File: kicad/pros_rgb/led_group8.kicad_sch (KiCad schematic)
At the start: 8 parts

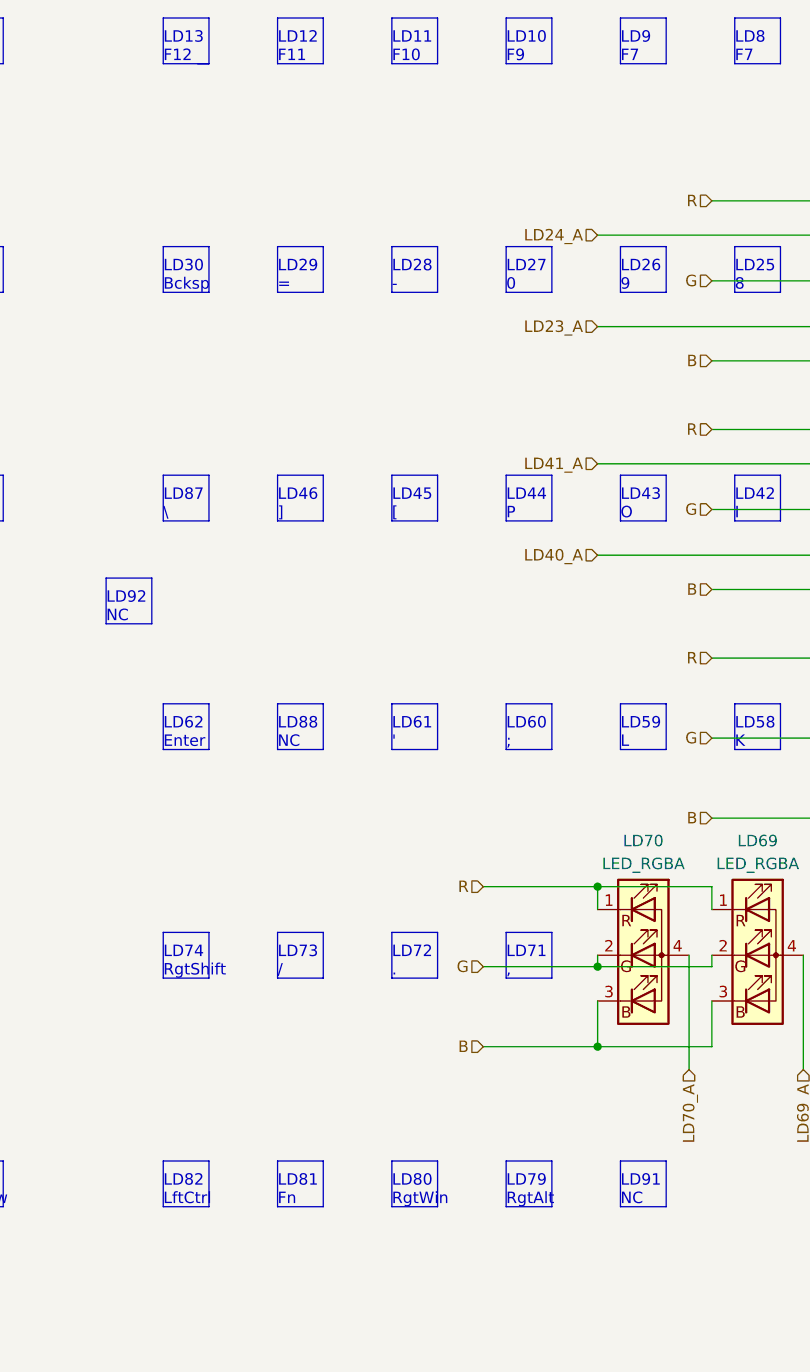
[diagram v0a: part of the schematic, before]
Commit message: kicad/pros_rgb: fix typos
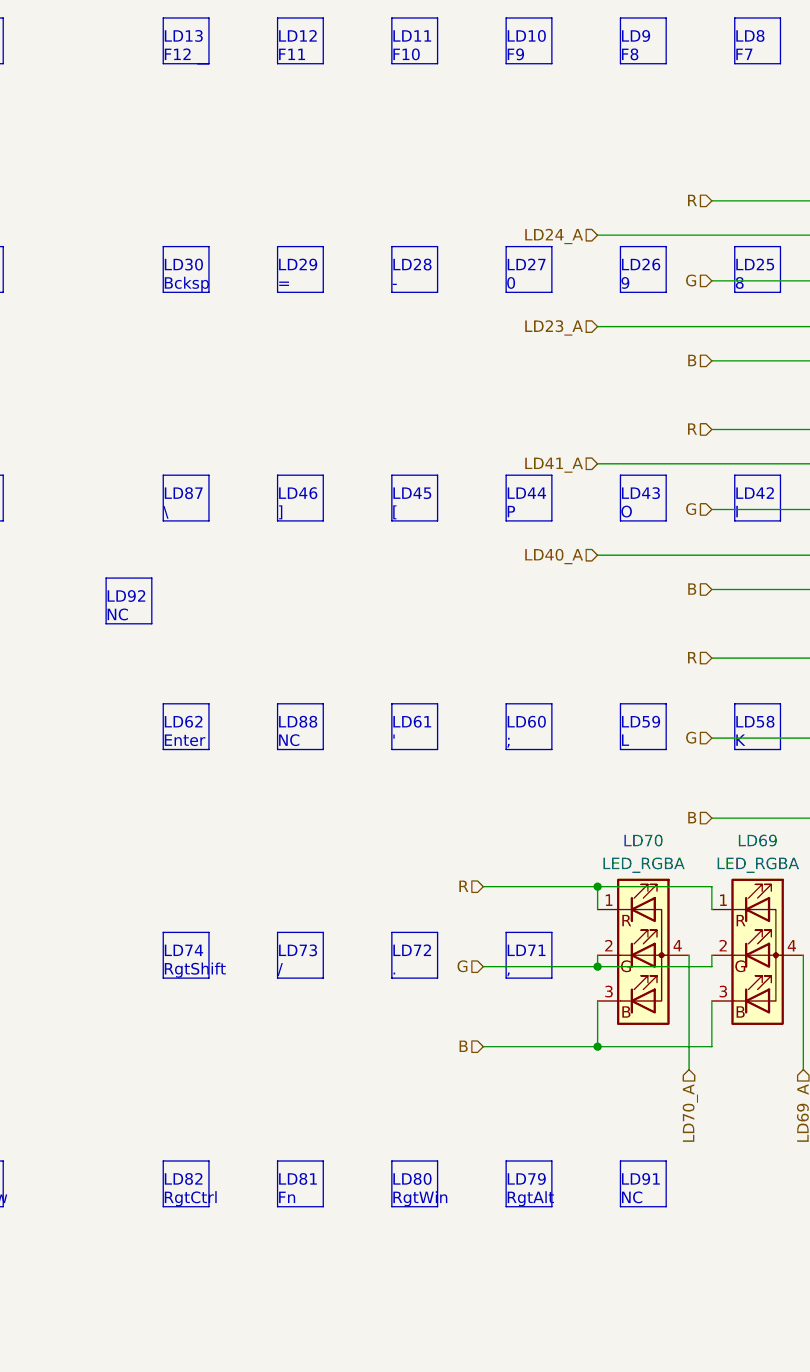
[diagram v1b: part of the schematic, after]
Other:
- note added: "LD82 RgtCtrl"
- note added: "LD9 F8"
- note removed: "LD82 LftCtrl"
- note removed: "LD9 F7"
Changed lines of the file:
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@@
     (effects (font (size 1.27 1.27)) (justify left bottom))
   )
-  (text "LD82\nLftCtrl" (at 106.68 156.21 0)
+  (text "LD82\nRgtCtrl" (at 106.68 156.21 0)
     (effects (font (size 1.27 1.27)) (justify left bottom))
   )
@@
     (effects (font (size 1.27 1.27)) (justify left bottom))
   )
-  (text "LD9\nF7" (at 157.48 29.21 0)
+  (text "LD9\nF8" (at 157.48 29.21 0)
     (effects (font (size 1.27 1.27)) (justify left bottom))
   )

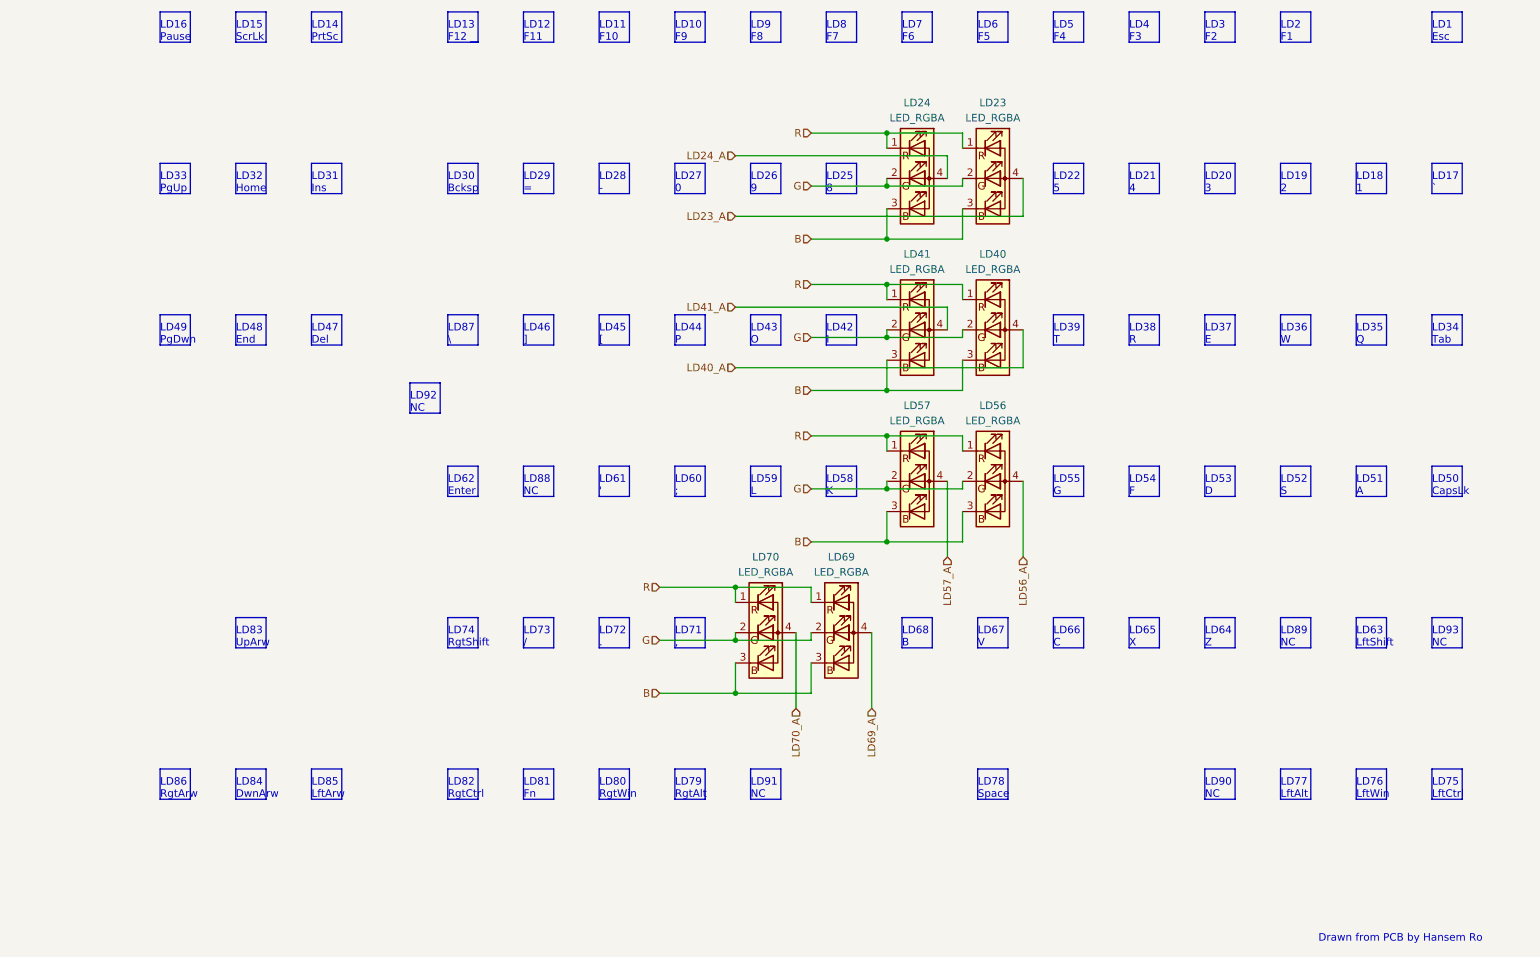
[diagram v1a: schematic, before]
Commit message: kicad/pros_rgb: order led groups by channel number
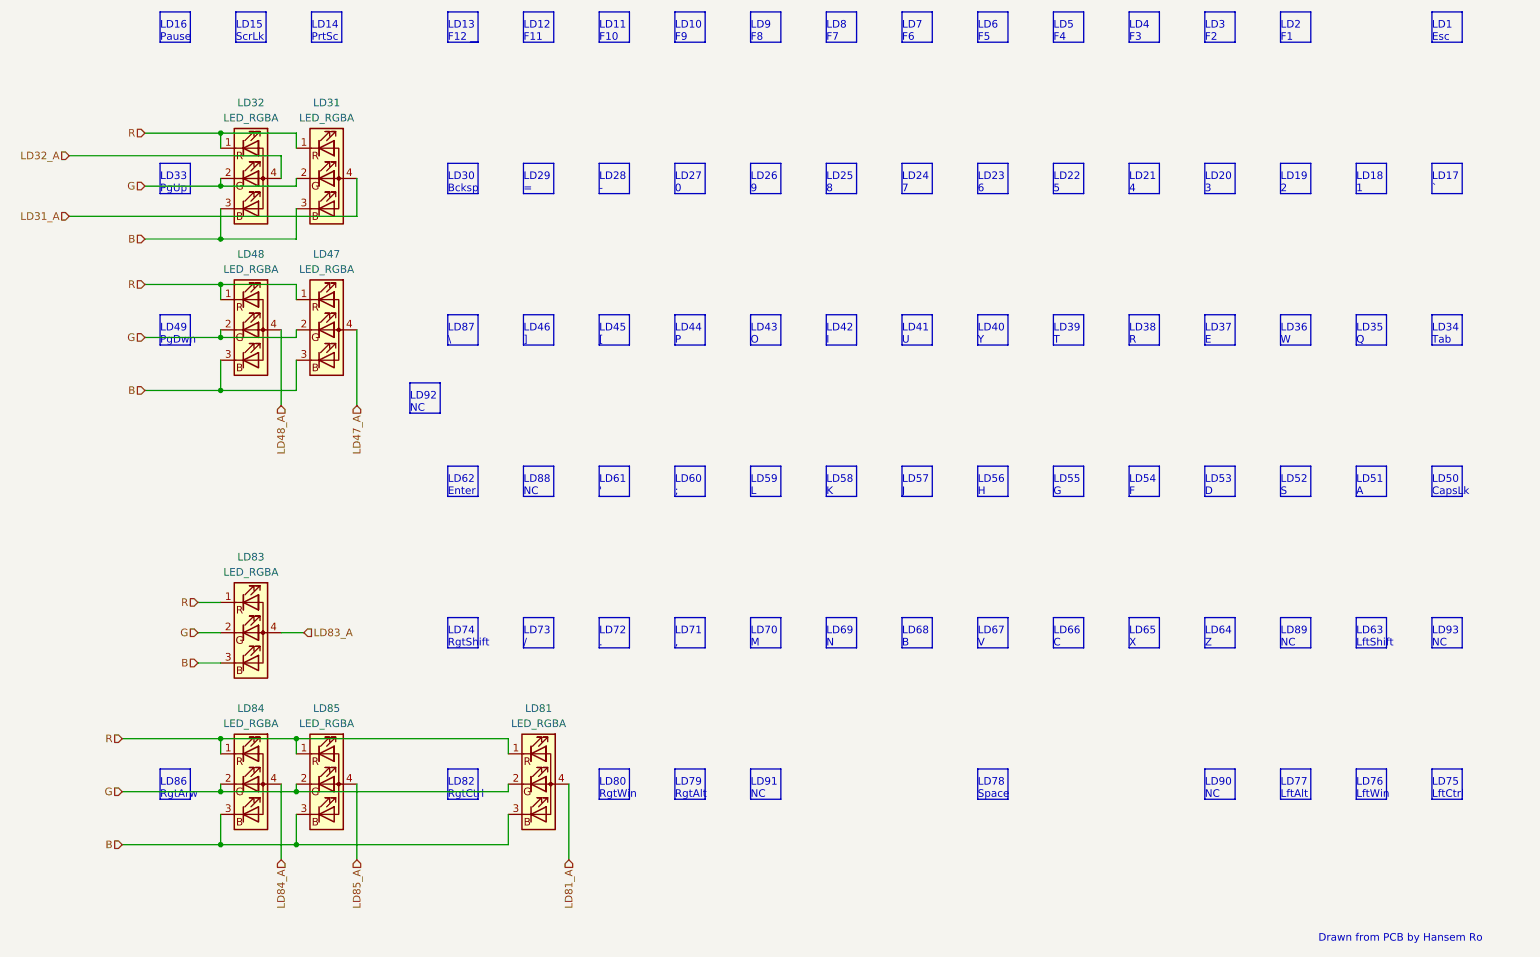
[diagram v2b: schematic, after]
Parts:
- removed LD23, LD24, LD40, LD41, LD56, LD57, LD69, LD70: LED_RGBA, symbol Device:LED_RGBA
- added LD31, LD32, LD47, LD48, LD81, LD83, LD84, LD85: LED_RGBA, symbol Device:LED_RGBA
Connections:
- net B: now also LD31.3 (BK), LD32.3 (BK), LD47.3 (BK), LD48.3 (BK), LD81.3 (BK), LD83.3 (BK), LD84.3 (BK), LD85.3 (BK)
- net G: now also LD31.2 (GK), LD32.2 (GK), LD47.2 (GK), LD48.2 (GK), LD81.2 (GK), LD83.2 (GK), LD84.2 (GK), LD85.2 (GK)
- net R: now also LD31.1 (RK), LD32.1 (RK), LD47.1 (RK), LD48.1 (RK), LD81.1 (RK), LD83.1 (RK), LD84.1 (RK), LD85.1 (RK)
- new net LD31_A: LD31.4 (A)
- new net LD32_A: LD32.4 (A)
- new net LD47_A: LD47.4 (A)
- new net LD48_A: LD48.4 (A)
- new net LD81_A: LD81.4 (A)
- new net LD83_A: LD83.4 (A)
- new net LD84_A: LD84.4 (A)
- new net LD85_A: LD85.4 (A)
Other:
- note added: "LD23 6"
- note added: "LD24 7"
- note added: "LD40 Y"
- note added: "LD41 U"
- note added: "LD56 H"
- note added: "LD57 J"
- note added: "LD69 N"
- note added: "LD70 M"
- note removed: "LD31 Ins"
- note removed: "LD32 Home"
- note removed: "LD47 Del"
- note removed: "LD48 End"
- note removed: "LD81 Fn"
- note removed: "LD83 UpArw"
- note removed: "LD84 DwnArw"
- note removed: "LD85 LftArw"
